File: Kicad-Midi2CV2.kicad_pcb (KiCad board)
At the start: 2 copper layers, 100 x 100 mm, 100 parts, among them IC101 MCP4725module, IC102 MCP4725module, J101 Doepfer connector, J102 Vin 7-12v, J103 MIDI OUT, J104 Power Conn, J105 CV7 in, J106 Gate1, J107 MIDI IN, J108 CV6 in, J109 Gate2, J110 CV3 in, J111 Gate3, J112 CV1, J113 Gate4, J114 CV2, J115 ControlConn, J116 ControlConn, J117 I2C_Conn, J118 I2C_Conn, Q101 MMBT2222A, Q102 MMBT2222A, SW101 KY40_Rotary_Encoder_Module, U101 TL072, U102 TL072, U103 EL814

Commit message: Sch and PCB advancements
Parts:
- added C118: 100n, Capacitor_SMD:C_0805_2012Metric_Pad1.15x1.40mm_HandSolder, B.Cu at (214.4, 85.4)
- added C119: 47n, Capacitor_SMD:C_0805_2012Metric_Pad1.15x1.40mm_HandSolder, B.Cu at (224.1, 92.2)
- added C120: 100n, Capacitor_SMD:C_0805_2012Metric_Pad1.15x1.40mm_HandSolder, B.Cu at (218.2, 85.4)
- added C121: 100n, Capacitor_SMD:C_0805_2012Metric_Pad1.15x1.40mm_HandSolder, B.Cu at (224.1, 90.2)
- added F101: Polyfuse, Fuse:Fuse_1206_3216Metric_Pad1.42x1.75mm_HandSolder, B.Cu at (151.5, 57.5)
- added R139: 680R, Resistor_SMD:R_0805_2012Metric_Pad1.15x1.40mm_HandSolder, B.Cu at (227.9, 92.2)
- added R140: 680R, Resistor_SMD:R_0805_2012Metric_Pad1.15x1.40mm_HandSolder, B.Cu at (221.9, 85.4)
- added R141: 680R, Resistor_SMD:R_0805_2012Metric_Pad1.15x1.40mm_HandSolder, B.Cu at (224.1, 88.3)
- added R142: 10k, Resistor_SMD:R_0805_2012Metric_Pad1.15x1.40mm_HandSolder, B.Cu at (227.9, 90.2)
- added R143: 10k, Resistor_SMD:R_0805_2012Metric_Pad1.15x1.40mm_HandSolder, B.Cu at (225.7, 86.3)
- added R144: 10k, Resistor_SMD:R_0805_2012Metric_Pad1.15x1.40mm_HandSolder, B.Cu at (227.9, 88.3)
- C102, C103, C104, C107, C108, C109, C111, C112, C113, C114, C116, C117, D101, D102, D103, F102, IC101, IC102, JP101, JP104, Q101, Q102, R101, R102, R103, R104, R105, R106, R107, R108, R109, R110, R111, R112, R113, R114, R115, R116, R117, R118, R120, R122, R123, R124, R125, R126, R127, R128, R129, R130, R131, R132, R135, U101, U102: moved to B.Cu
- C115: value 10n -> 100n; moved to B.Cu
- J115: footprint Connector_PinHeader_2.54mm:PinHeader_1x12_P2.54mm_Vertical -> Connector_PinHeader_2.54mm:PinHeader_1x11_P2.54mm_Vertical
- J116: footprint Connector_PinHeader_2.54mm:PinHeader_1x12_P2.54mm_Horizontal -> Connector_PinHeader_2.54mm:PinHeader_1x11_P2.54mm_Vertical
- J117: footprint Connector_PinHeader_2.54mm:PinHeader_1x08_P2.54mm_Vertical -> Connector_PinHeader_2.54mm:PinHeader_1x09_P2.54mm_Vertical
- J118: footprint Connector_PinHeader_2.54mm:PinHeader_1x08_P2.54mm_Horizontal -> Connector_PinHeader_2.54mm:PinHeader_1x09_P2.54mm_Vertical
- R119: value 10k -> 220R; moved to B.Cu
- R121: value 220R -> 10k; moved to B.Cu
- R133, R134, R136, R137: value 680R -> 10k; moved to B.Cu
- R138: value 10k -> 680R; moved to B.Cu
- SW101: value KY40_Rotary_Encoder_Module -> Rotary_Encoder_Switch; footprint Rotary_Encoder:KY-40-rotary-encoder-board -> Rotary_Encoder:RotaryEncoder_Alps_EC11E-Switch_Vertical_H20mm
- moved R138 189.5 mm to (121.5, 126.5)
- moved D110 184.7 mm to (108.0, 131.5)
- moved R136 180.5 mm to (115.0, 130.0), turned to 180 degrees
- moved R105 167.8 mm to (115.0, 135.0), turned to 180 degrees
- moved D108 166.3 mm to (120.0, 122.0), turned to 0 degrees
- moved J110 164.9 mm to (194.5, 123.5)
- moved R134 162.6 mm to (120.9, 118.0), turned to 90 degrees
- moved IC101 160.5 mm to (115.8, 113.8)
- moved C111 155.4 mm to (108.8, 111.2)
- moved R112 145.3 mm to (102.5, 106.1)
- moved A101 144.5 mm to (164.0, 145.5)
- moved U101 140.2 mm to (108.8, 103.6), turned to 90 degrees
- moved SW101 135.6 mm to (120.0, 67.5), turned to 90 degrees
- moved R104 128.7 mm to (105.0, 96.0)
- moved C107 126.2 mm to (109.4, 96.0)
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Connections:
- C115 pad 1: Btn -> Gate3Gain
- C115 pad 2: GND -> Net-(C115-Pad2)
- C116 pad 1: A1 -> Net-(C116-Pad1)
- C117 pad 1: A2 -> Gate4Gain
- C117 pad 2: GND -> Net-(C117-Pad2)
- J104 pad 1: +12V -> -12V
- J104 pad 2: -12V -> GND
- J104 pad 3: VCC -> +12V
- J104 pad 4: Net-(A101-Pad17) -> +5V
- J104 pad 5: +5V -> VCC
- J104 pad 6: GND -> Net-(A101-Pad17)
- J115 pad 1: GND -> Gate1
- J115 pad 10: LED-CV2 -> LED2
- J115 pad 11: LED-CV1 -> LED1
- J115 pad 2: A2 -> Gate2
- J115 pad 3: A1 -> Net-(J115-Pad3)
- J115 pad 4: Btn -> LED_LFO
- J115 pad 5: LED_LFO -> LED-CV2
- J115 pad 6: LED4 -> LED-CV1
- J115 pad 7: LED3 -> LED-MIDI
- J115 pad 8: LED2 -> LED4
- J115 pad 9: LED1 -> LED3
- J116 pad 1: GND -> Gate1
- J116 pad 10: LED-CV2 -> LED2
- J116 pad 11: LED-CV1 -> LED1
- J116 pad 2: A2 -> Gate2
- J116 pad 3: A1 -> Net-(J115-Pad3)
- J116 pad 4: Btn -> LED_LFO
- J116 pad 5: LED_LFO -> LED-CV2
- J116 pad 6: LED4 -> LED-CV1
- J116 pad 7: LED3 -> LED-MIDI
- J116 pad 8: LED2 -> LED4
- J116 pad 9: LED1 -> LED3
- J117 pad 3: SCL -> Btn
- J117 pad 4: SDA -> A1
- J117 pad 5: Gate1 -> A2
- J117 pad 6: Gate2 -> SDA
- J117 pad 7: +5V -> SCL
- J117 pad 8: +12V -> +5V
- J118 pad 3: SCL -> Btn
- J118 pad 4: SDA -> A1
- J118 pad 5: Gate1 -> A2
- J118 pad 6: Gate2 -> SDA
- J118 pad 7: +5V -> SCL
- J118 pad 8: +12V -> +5V
- R118 pad 1: Net-(R118-Pad1) -> Net-(J105-PadT)
- R118 pad 2: GND -> A7
- R119 pad 1: Gate3Gain -> Net-(D103-Pad1)
- R119 pad 2: Net-(R118-Pad1) -> Net-(J107-Pad4)
- R120 pad 1: Net-(J105-PadT) -> A7
- R120 pad 2: A7 -> Net-(J105-PadS)
- R121 pad 1: Net-(D103-Pad1) -> Net-(R121-Pad1)
- R121 pad 2: Net-(J107-Pad4) -> GND
- R122 pad 1: A7 -> Gate3Gain
- R122 pad 2: Net-(J105-PadS) -> Net-(R121-Pad1)
- R126 pad 1: Net-(J110-PadT) -> Net-(C115-Pad2)
- R126 pad 2: A3 -> Gate3
- R127 pad 1: A3 -> Net-(C116-Pad1)
- R127 pad 2: Net-(J105-PadS) -> Net-(C115-Pad2)
- R128 pad 1: Net-(R128-Pad1) -> Net-(J110-PadT)
- R128 pad 2: GND -> A3
- R129 pad 1: Gate4Gain -> A3
- R129 pad 2: Net-(R128-Pad1) -> Net-(J105-PadS)
- R133 pad 1: LED4 -> Net-(R133-Pad1)
- R133 pad 2: Net-(D107-Pad2) -> GND
- R134 pad 1: LED-MIDI -> Gate4Gain
- R134 pad 2: Net-(D108-Pad2) -> Net-(R133-Pad1)
- R135 pad 1: LED_LFO -> LED4
- R135 pad 2: Net-(D109-Pad2) -> Net-(D107-Pad2)
- R136 pad 1: LED-CV1 -> Net-(C117-Pad2)
- R136 pad 2: Net-(D110-Pad2) -> Gate4
- R137 pad 1: LED-CV2 -> Net-(C118-Pad1)
- R137 pad 2: Net-(D111-Pad2) -> Net-(C117-Pad2)
- R138 pad 1: Btn -> LED-MIDI
- R138 pad 2: Net-(R138-Pad2) -> Net-(D108-Pad2)
- RV101 pad 2: CV2Gain -> CV1Gain
- RV101 pad 3: CV2Gain -> CV1Gain
- RV102 pad 2: CV1Gain -> CV2Gain
- RV102 pad 3: CV1Gain -> CV2Gain
- U101 pad 1: CV1Gain -> CV2Gain
- U101 pad 3: CV1 -> CV2
- U101 pad 5: CV2 -> CV1
- U101 pad 7: CV2Gain -> CV1Gain
- U102 pad 1: Gate4Gain -> Gate3Gain
- U102 pad 2: Net-(R128-Pad1) -> Net-(R121-Pad1)
- U102 pad 3: Gate4 -> Net-(C116-Pad1)
- U102 pad 5: Gate3 -> Net-(C118-Pad1)
- U102 pad 6: Net-(R118-Pad1) -> Net-(R133-Pad1)
- U102 pad 7: Gate3Gain -> Gate4Gain
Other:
- outline, holes or cut-outs redrawn
- board text added: "+3 VCC +5 +12 GND -12"
- board text added: "-12 GND A0 A1 A2 A4 A5 +5 +12"
- board text added: "-12 GND BTN A1 A2 SDA SCL +5 +12"
- board text added: "D6 D7 GND D13 D12 D11 D10 D5 D4 D3 D2"
- board text added: "G1 G2 GND LFO CV2 CV1 MIDI 4 3 2 1"
- board text added: "PROMESOFT Johansen Engineering MIDI2CV MK2.1 Rev A 2019W05"
- board text added: "PROMESOFT Johansen Enginerring SubSection - 2019W05 DAC Gate CV MK2.1RevA"
- board text removed: "D6 D7 D8 D9 A6 A7"
- board text removed: "G1 G2 G3 G4 CV6 CV7"
- board text removed: "GND A5 A4 D12 D13 5V"
- board text removed: "PROMESOFT Johansen Engineering MIDI2CV Rev B 2019W03"
- board text removed: "PROMESOFT Johansen Enginerring SubSection - 2019W03 DAC Gate CV RevB"

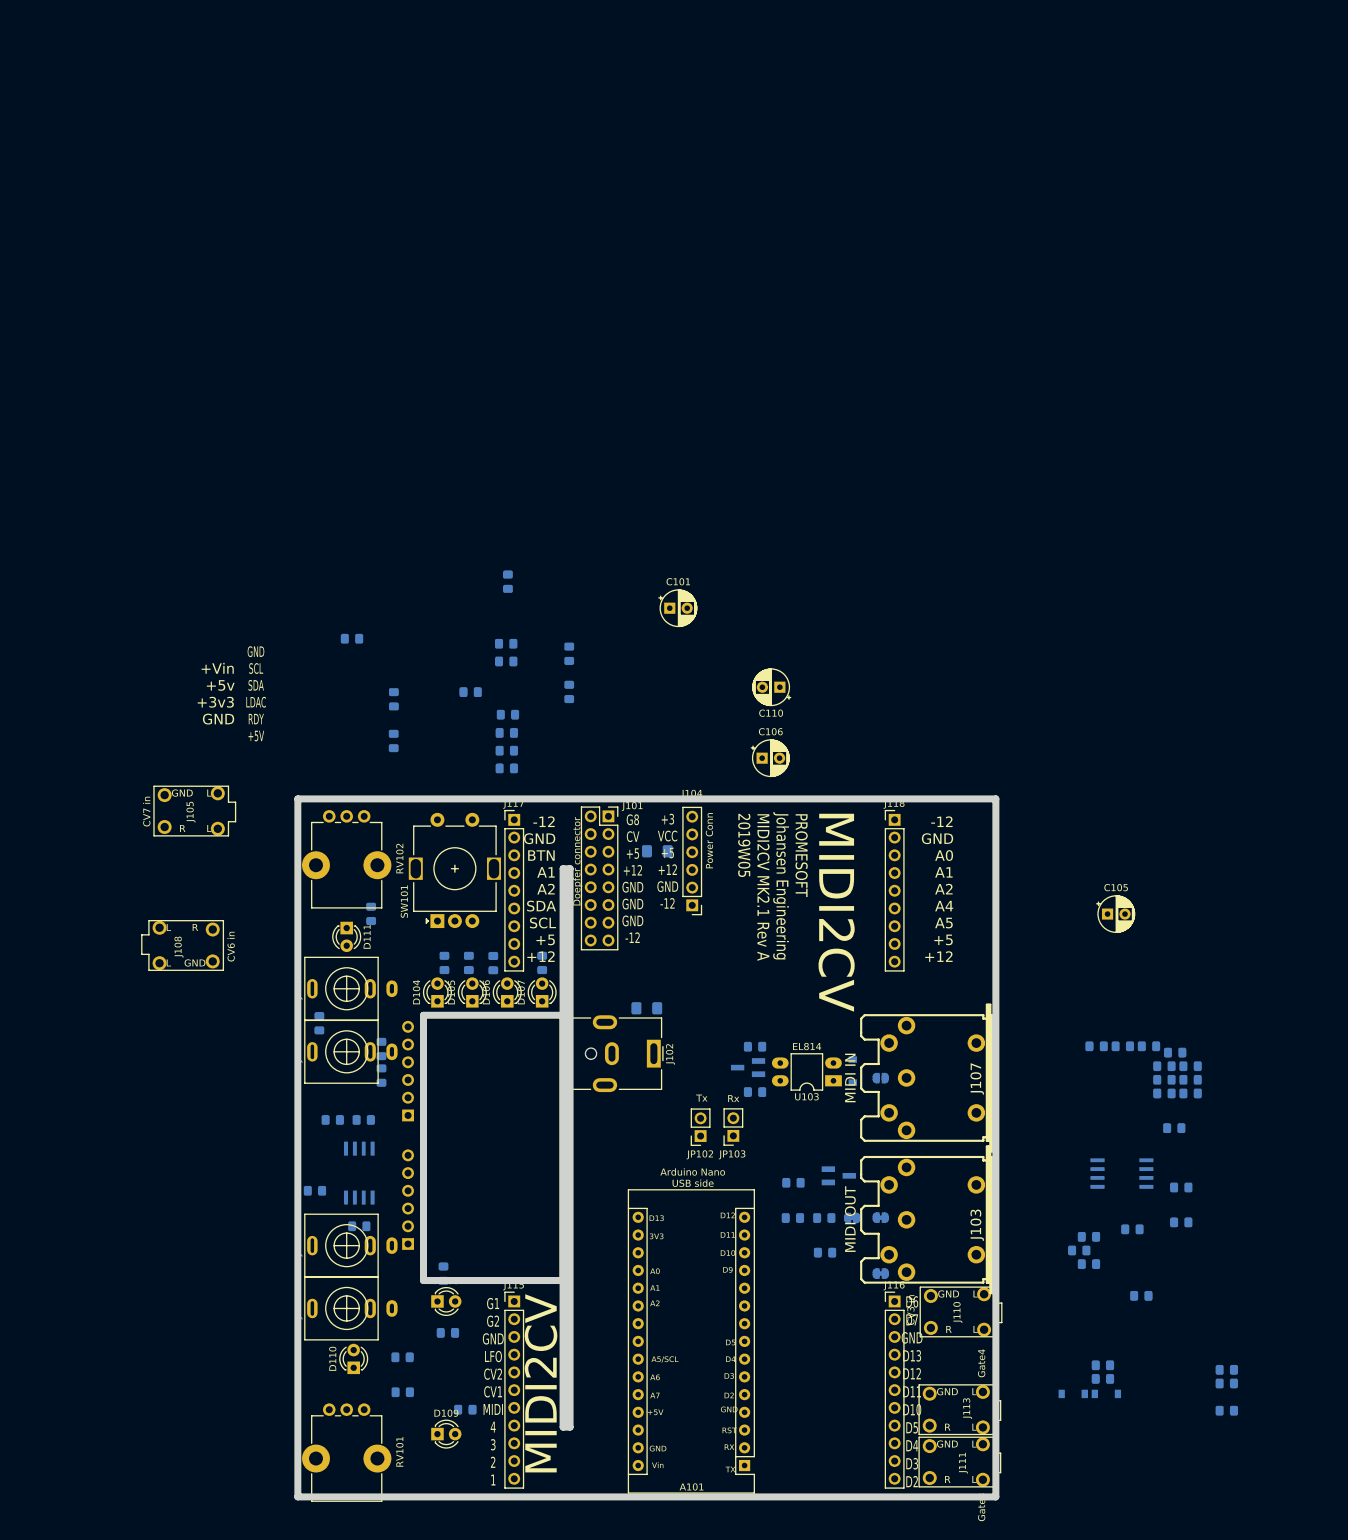
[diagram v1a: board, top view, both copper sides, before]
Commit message: RC output on CV
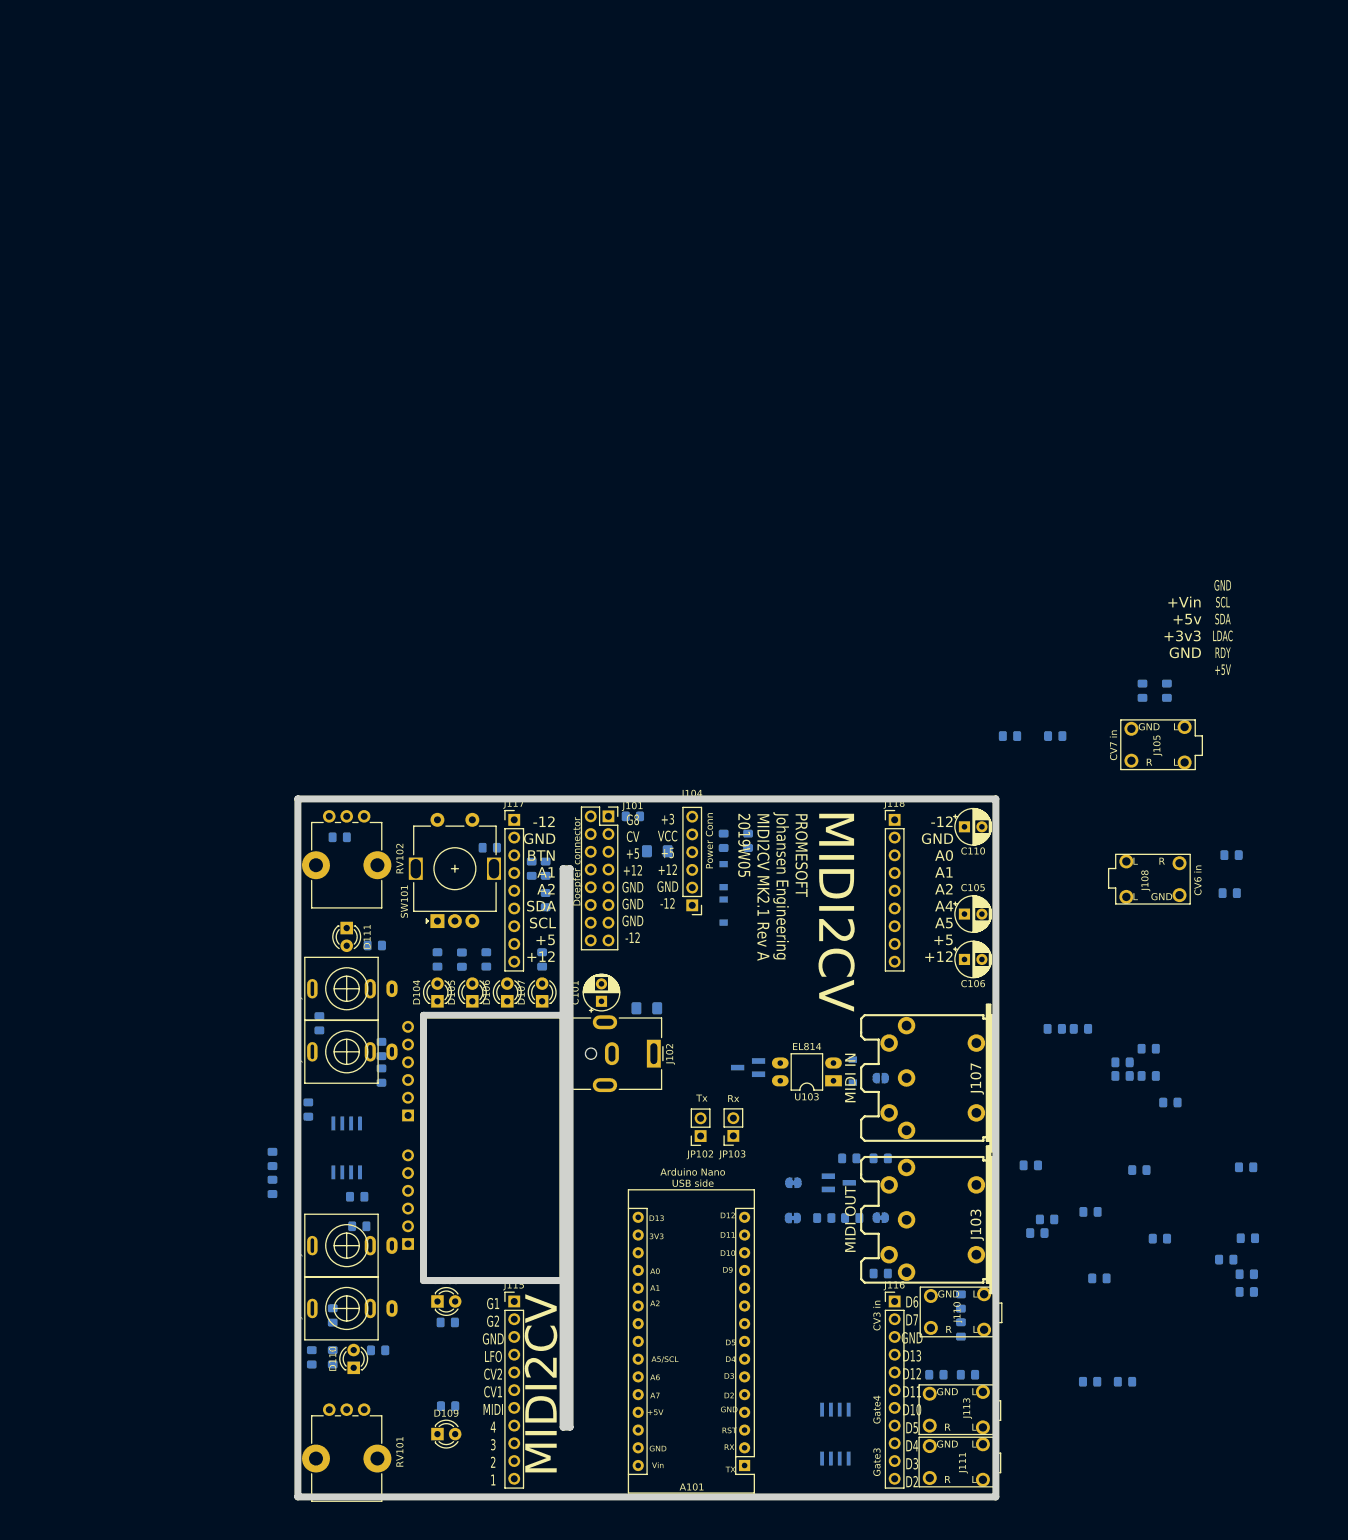
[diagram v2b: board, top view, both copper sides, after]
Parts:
- added C122: 100n, Capacitor_SMD:C_0805_2012Metric_Pad1.15x1.40mm_HandSolder, B.Cu at (133.5, 60.0)
- added C123: 100n, Capacitor_SMD:C_0805_2012Metric_Pad1.15x1.40mm_HandSolder, B.Cu at (135.5, 60.0)
- added R145: 10k, Resistor_SMD:R_0805_2012Metric_Pad1.15x1.40mm_HandSolder, B.Cu at (135.5, 64.5)
- added R146: 10k, Resistor_SMD:R_0805_2012Metric_Pad1.15x1.40mm_HandSolder, B.Cu at (127.5, 57.0)
- C114, C115, C121: value 100n -> 47n
- C119: value 47n -> 100n
- R108: value OPEN -> 100R
- R109: value 220R -> OPEN
- R110: value 0R -> 220R; footprint Jumper:SolderJumper-2_P1.3mm_Bridged_RoundedPad1.0x1.5mm -> Resistor_SMD:R_0805_2012Metric_Pad1.15x1.40mm_HandSolder
- R111: value OPEN -> 0R; footprint Resistor_SMD:R_0805_2012Metric_Pad1.15x1.40mm_HandSolder -> Jumper:SolderJumper-2_P1.3mm_Bridged_RoundedPad1.0x1.5mm
- R112: value 10k -> OPEN
- R114: value 0R -> 10k; footprint Jumper:SolderJumper-2_P1.3mm_Bridged_RoundedPad1.0x1.5mm -> Resistor_SMD:R_0805_2012Metric_Pad1.15x1.40mm_HandSolder
- R115: value 2k -> 0R; footprint Resistor_SMD:R_0805_2012Metric_Pad1.15x1.40mm_HandSolder -> Jumper:SolderJumper-2_P1.3mm_Bridged_RoundedPad1.0x1.5mm
- R116: value 680R -> 2k
- R117: value 1k -> 680R
- R118: value 10k -> 100R
- R119: value 220R -> 1k
- R121: value 10k -> 220R
- R124: value 1k -> 10k
- R126: value 10k -> 1k
- R130, R131, R135, R138, R139: value 680R -> 10k
- R133, R134, R137, R142, R143: value 10k -> 680R
- moved R118 149.2 mm to (106.0, 55.5)
- moved C112 140.4 mm to (96.4, 105.6), turned to 90 degrees
- moved J105 138.8 mm to (223.2, 42.2)
- moved J108 138.8 mm to (222.5, 61.5)
- moved C115 129.8 mm to (235.9, 120.6)
- moved C116 129.8 mm to (235.9, 118.1)
- moved R122 129.8 mm to (235.8, 102.8)
- moved R127 129.8 mm to (236.1, 112.9)
- moved R123 129.8 mm to (233.8, 58.1)
- moved C117 127.7 mm to (233.0, 116.0)
- moved R126 126.0 mm to (223.5, 113.0)
- moved R142 122.7 mm to (111.5, 129.0), turned to 180 degrees
- moved R143 115.7 mm to (111.0, 71.0)
- moved R141 113.6 mm to (121.5, 137.0)
- moved R102 110.8 mm to (224.5, 34.5)
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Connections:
- C114 pad 1: GND -> CV1Gain
- C114 pad 2: +5V -> GND
- C115 pad 1: Gate3Gain -> CV2Gain
- C115 pad 2: Net-(C115-Pad2) -> GND
- C116 pad 1: Net-(C116-Pad1) -> GND
- C116 pad 2: GND -> +5V
- C117 pad 1: Gate4Gain -> Gate3Gain
- C119 pad 1: Btn -> Gate4Gain
- C119 pad 2: GND -> Net-(C119-Pad2)
- C120 pad 1: A1 -> Net-(C120-Pad1)
- C121 pad 1: A2 -> Btn
- J105 pad S: Net-(J105-PadS) -> GND
- J106 pad S: GND -> Net-(J106-PadS)
- J108 pad S: Net-(J105-PadS) -> GND
- J109 pad S: GND -> Net-(J106-PadS)
- J110 pad S: Net-(J105-PadS) -> GND
- J111 pad S: GND -> Net-(J106-PadS)
- J112 pad S: Net-(J105-PadS) -> GND
- J113 pad S: GND -> Net-(J106-PadS)
- J114 pad S: Net-(J105-PadS) -> GND
- R108 pad 1: /MIDI-OUT-5 -> CV1Gain
- R108 pad 2: +5V -> Net-(R108-Pad2)
- R109 pad 1: /MIDI-OUT-4 -> /MIDI-OUT-5
- R110 pad 1: /Q1Coll -> /MIDI-OUT-4
- R111 pad 1: /Q1Emitter -> /Q1Coll
- R111 pad 2: /MIDI-OUT-4 -> +5V
- R112 pad 1: Net-(R112-Pad1) -> /Q1Emitter
- R112 pad 2: GND -> /MIDI-OUT-4
- R113 pad 2: Net-(R112-Pad1) -> GND
- R114 pad 1: /Q1Emitter -> Net-(R114-Pad1)
- R114 pad 2: /MIDI-OUT-5 -> Net-(R113-Pad1)
- R115 pad 1: /TX -> /Q1Emitter
- R115 pad 2: /Q1Base -> /MIDI-OUT-5
- R116 pad 1: /Q1Emitter -> /TX
- R116 pad 2: GND -> /Q1Base
- R117 pad 1: /Q2Coll -> /Q1Emitter
- R117 pad 2: +5V -> GND
- R118 pad 1: Net-(J105-PadT) -> CV2Gain
- R118 pad 2: A7 -> Net-(R118-Pad2)
- R119 pad 1: Net-(D103-Pad1) -> /Q2Coll
- R119 pad 2: Net-(J107-Pad4) -> +5V
- R120 pad 1: A7 -> Net-(J105-PadT)
- R120 pad 2: Net-(J105-PadS) -> A7
- R121 pad 1: Net-(R121-Pad1) -> Net-(D103-Pad1)
- R121 pad 2: GND -> Net-(J107-Pad4)
- R122 pad 1: Gate3Gain -> A7
- R122 pad 2: Net-(R121-Pad1) -> GND
- R123 pad 1: Net-(J108-PadT) -> Net-(R123-Pad1)
- R123 pad 2: A6 -> GND
- R124 pad 1: GND -> Gate3Gain
- R124 pad 2: /MIDI-IN -> Net-(R123-Pad1)
- R125 pad 1: A6 -> Net-(J108-PadT)
- R125 pad 2: Net-(J105-PadS) -> A6
- R126 pad 1: Net-(C115-Pad2) -> GND
- R126 pad 2: Gate3 -> /MIDI-IN
- R127 pad 1: Net-(C116-Pad1) -> A6
- R127 pad 2: Net-(C115-Pad2) -> GND
- R128 pad 1: Net-(J110-PadT) -> Net-(C117-Pad2)
- R128 pad 2: A3 -> Gate3
- R129 pad 1: A3 -> Net-(C118-Pad1)
- R129 pad 2: Net-(J105-PadS) -> Net-(C117-Pad2)
- R130 pad 1: LED1 -> Net-(J110-PadT)
- R130 pad 2: Net-(D104-Pad2) -> A3
- R131 pad 1: LED2 -> A3
- R131 pad 2: Net-(D105-Pad2) -> GND
- R132 pad 1: LED3 -> LED1
- R132 pad 2: Net-(D106-Pad2) -> Net-(D104-Pad2)
- R133 pad 1: Net-(R133-Pad1) -> LED2
- R133 pad 2: GND -> Net-(D105-Pad2)
- R134 pad 1: Gate4Gain -> LED3
- R134 pad 2: Net-(R133-Pad1) -> Net-(D106-Pad2)
- R135 pad 1: LED4 -> Net-(R135-Pad1)
- R135 pad 2: Net-(D107-Pad2) -> GND
- R136 pad 1: Net-(C117-Pad2) -> Gate4Gain
- R136 pad 2: Gate4 -> Net-(R135-Pad1)
- R137 pad 1: Net-(C118-Pad1) -> LED4
- R137 pad 2: Net-(C117-Pad2) -> Net-(D107-Pad2)
- R138 pad 1: LED-MIDI -> Net-(C119-Pad2)
- R138 pad 2: Net-(D108-Pad2) -> Gate4
- R139 pad 1: LED_LFO -> Net-(C120-Pad1)
- R139 pad 2: Net-(D109-Pad2) -> Net-(C119-Pad2)
- R140 pad 1: LED-CV1 -> LED-MIDI
- R140 pad 2: Net-(D110-Pad2) -> Net-(D108-Pad2)
- R141 pad 1: LED-CV2 -> LED_LFO
- R141 pad 2: Net-(D111-Pad2) -> Net-(D109-Pad2)
- R142 pad 1: +5V -> LED-CV1
- R142 pad 2: A1 -> Net-(D110-Pad2)
- R143 pad 1: A2 -> LED-CV2
- R143 pad 2: +5V -> Net-(D111-Pad2)
- R144 pad 1: Btn -> +5V
- R144 pad 2: Net-(R144-Pad2) -> A1
- RV101 pad 2: CV1Gain -> Net-(R108-Pad2)
- RV101 pad 3: CV1Gain -> Net-(R108-Pad2)
- RV102 pad 1: Net-(R113-Pad1) -> Net-(R114-Pad1)
- RV102 pad 2: CV2Gain -> Net-(R118-Pad2)
- RV102 pad 3: CV2Gain -> Net-(R118-Pad2)
- SW101 pad S1: Net-(R144-Pad2) -> Net-(R146-Pad2)
- U101 pad 1: CV2Gain -> Net-(R118-Pad2)
- U101 pad 2: Net-(R112-Pad1) -> Net-(R113-Pad1)
- U101 pad 7: CV1Gain -> Net-(R108-Pad2)
- U102 pad 2: Net-(R121-Pad1) -> Net-(R123-Pad1)
- U102 pad 3: Net-(C116-Pad1) -> Net-(C118-Pad1)
- U102 pad 5: Net-(C118-Pad1) -> Net-(C120-Pad1)
- U102 pad 6: Net-(R133-Pad1) -> Net-(R135-Pad1)
